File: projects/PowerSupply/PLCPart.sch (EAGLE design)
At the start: 29 parts, among them IC1 L7818CV, IC2 L7918CV, IC3 LM741P, IC4 LM741P, IC5 L7915CV, IC6 L7815CV, X1 MCU-PWR, X2 MCU-IN, X3 MCU-OUT

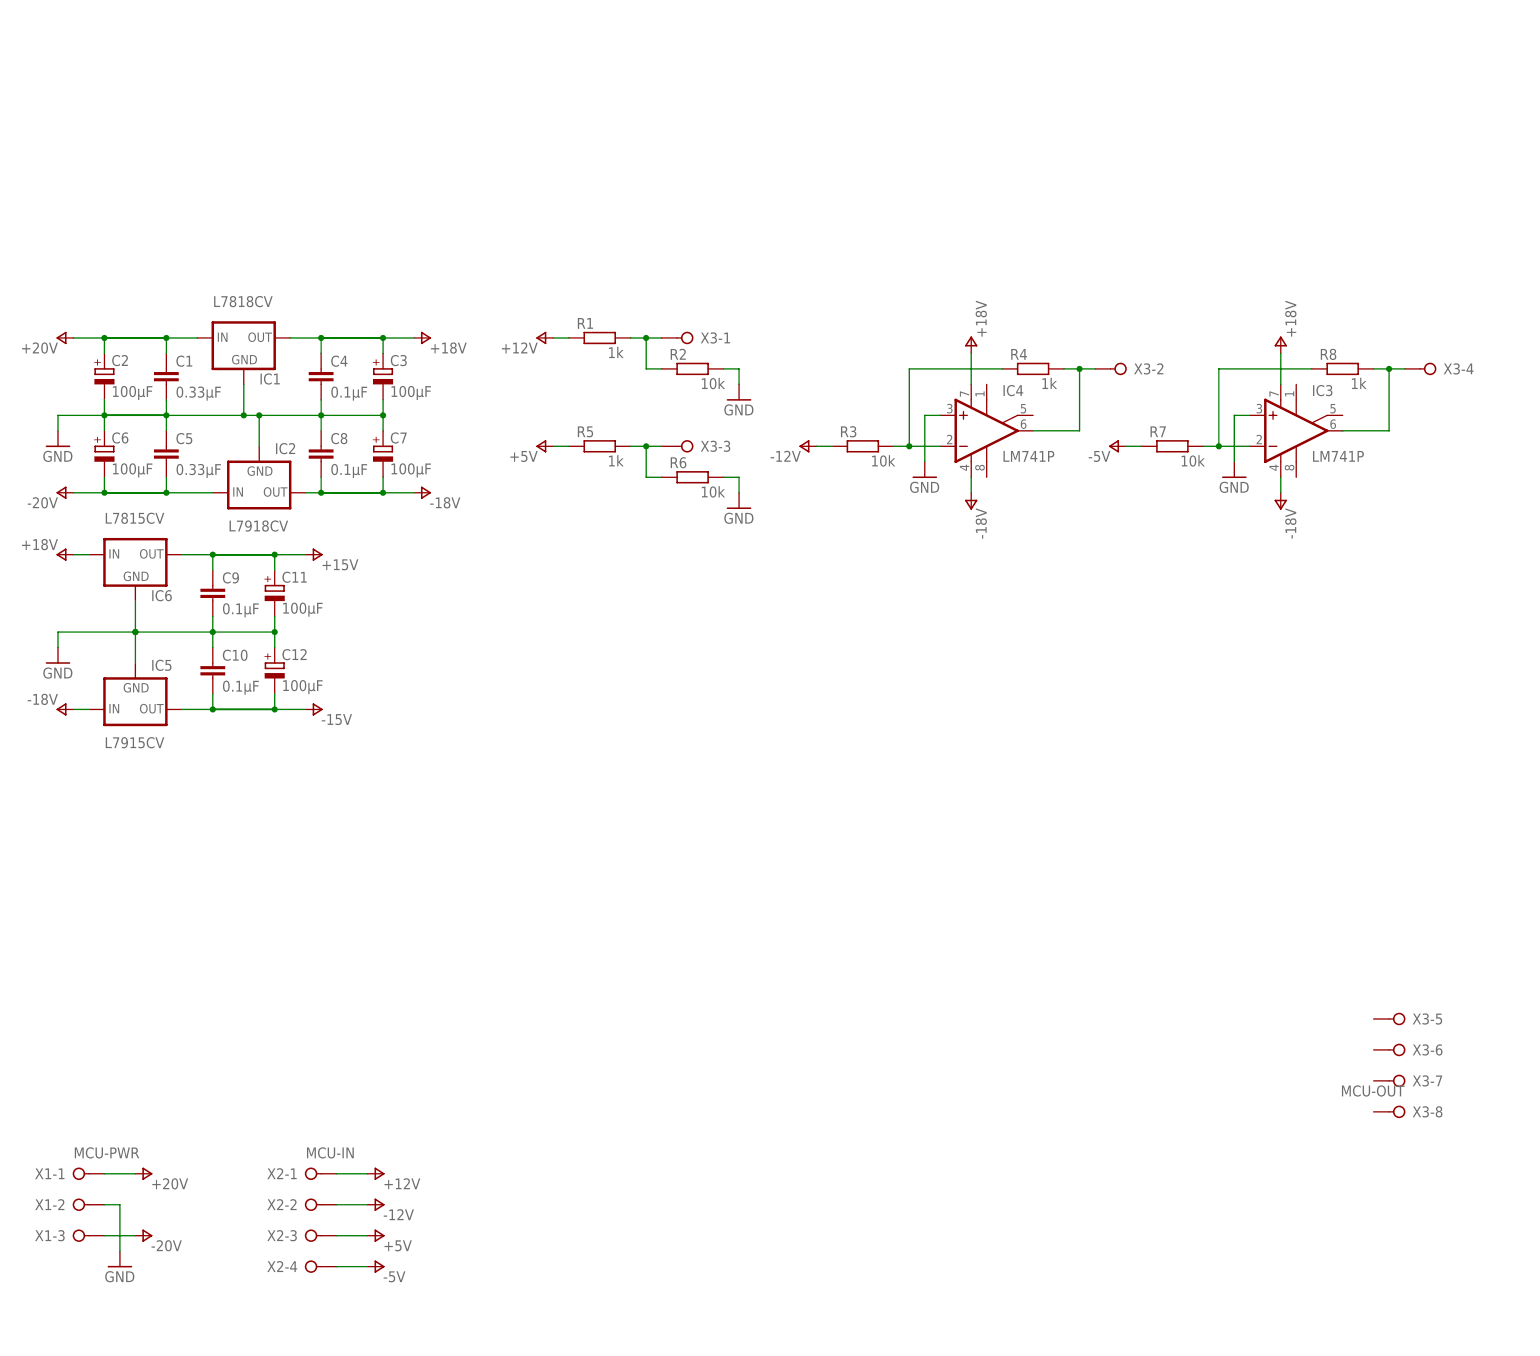
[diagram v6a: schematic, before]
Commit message: feat: plc part op amps (lm358) added
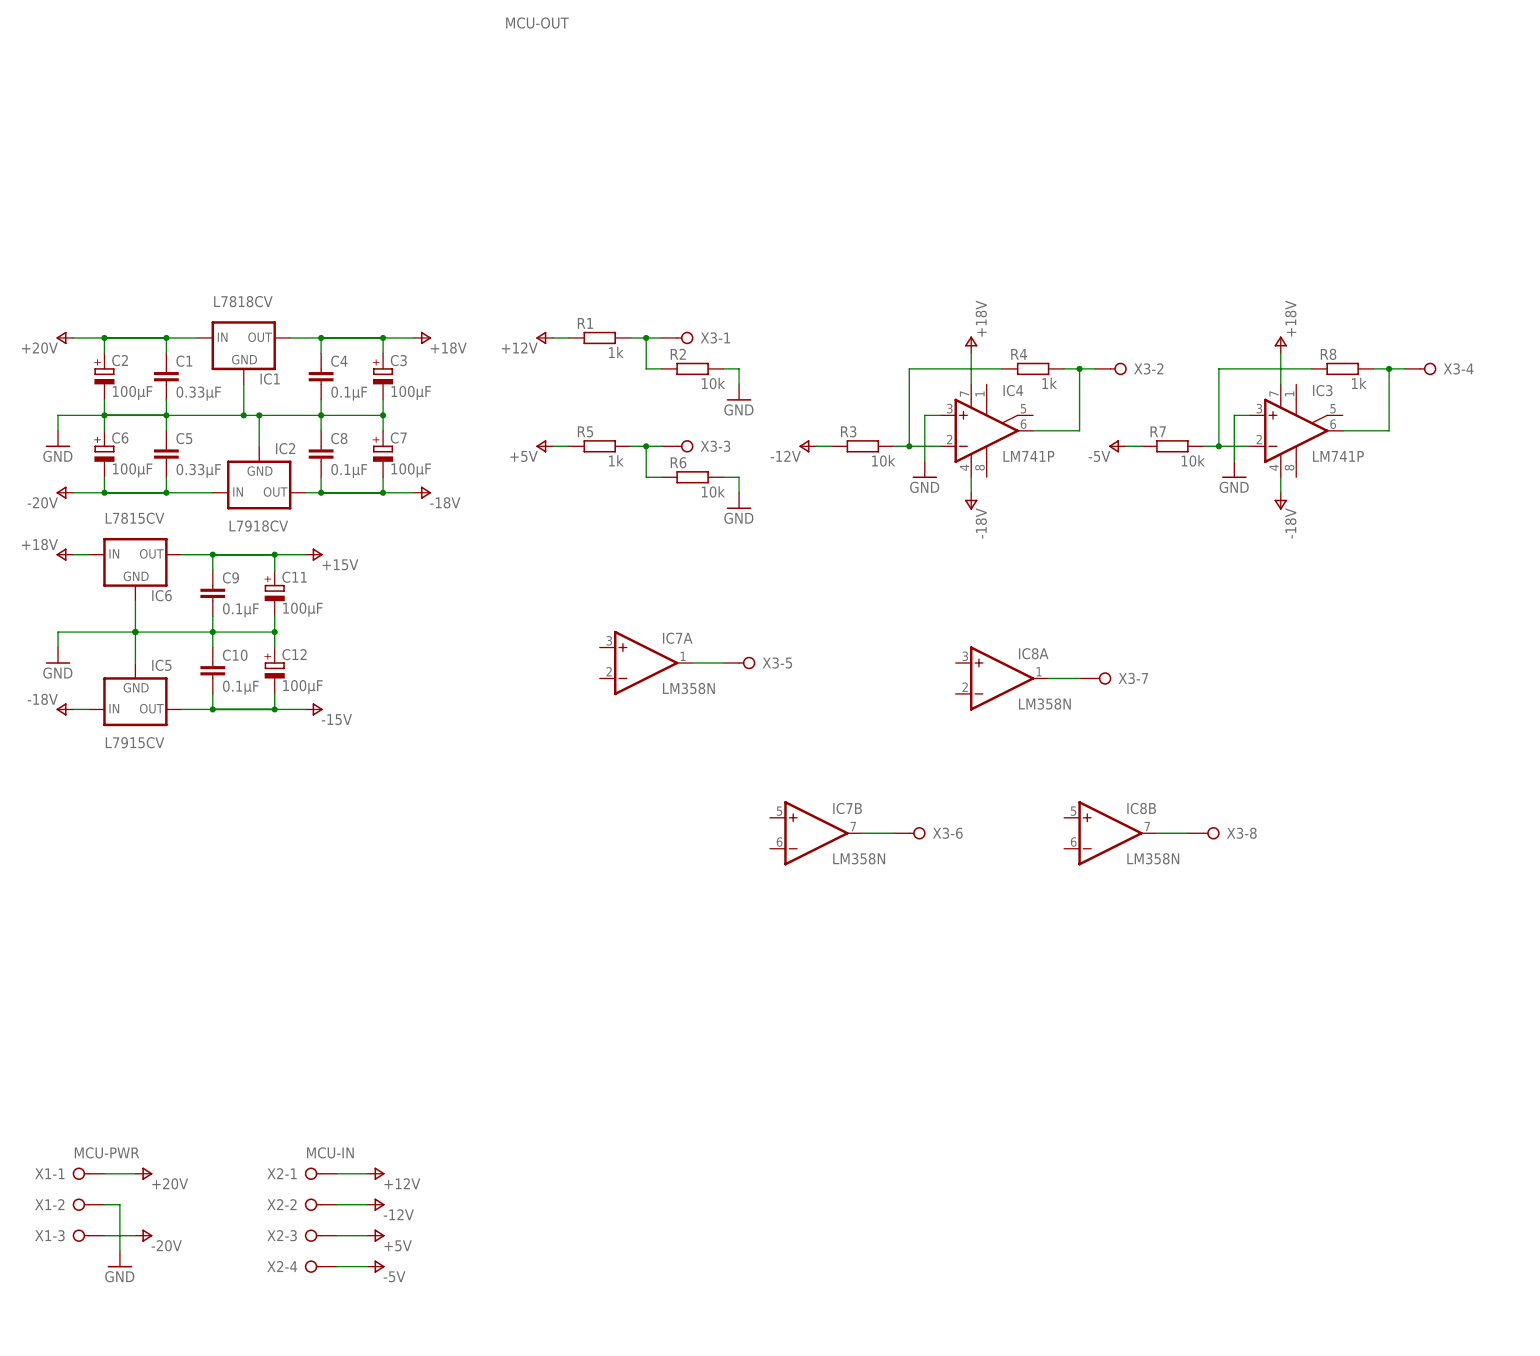
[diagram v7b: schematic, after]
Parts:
- added IC7, IC8: LM358N, linear:LM358N
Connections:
- new net N$10: IC8B.OUT, X3-8.KL
- new net N$7: IC7A.OUT, X3-5.KL
- new net N$8: IC7B.OUT, X3-6.KL
- new net N$9: IC8A.OUT, X3-7.KL
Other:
- moved on the sheet: X3-5, X3-6, X3-7, X3-8
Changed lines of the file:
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@@
 <part name="P+10" library="bb84-supply" deviceset="+15V" device=""/>
 <part name="P-10" library="bb84-supply" deviceset="-15V" device=""/>
+<part name="IC7" library="linear" library_urn="urn:adsk.eagle:library:262" deviceset="LM358" device="N" package3d_urn="urn:adsk.eagle:package:16409/2"/>
+<part name="IC8" library="linear" library_urn="urn:adsk.eagle:library:262" deviceset="LM358" device="N" package3d_urn="urn:adsk.eagle:package:16409/2"/>
 </parts>
 <sheets>
@@
 <attribute name="NAME" x="242.57" y="163.449" size="1.778" layer="95" rot="MR180"/>
 </instance>
-<instance part="X3" gate="-5" x="236.22" y="55.88" smashed="yes" rot="MR0">
-<attribute name="NAME" x="237.49" y="56.769" size="1.778" layer="95" rot="MR180"/>
-</instance>
-<instance part="X3" gate="-6" x="236.22" y="50.8" smashed="yes" rot="MR0">
-<attribute name="NAME" x="237.49" y="51.689" size="1.778" layer="95" rot="MR180"/>
-</instance>
-<instance part="X3" gate="-7" x="236.22" y="45.72" smashed="yes" rot="MR0">
-<attribute name="NAME" x="237.49" y="46.609" size="1.778" layer="95" rot="MR180"/>
-</instance>
-<instance part="X3" gate="-8" x="236.22" y="40.64" smashed="yes" rot="MR0">
-<attribute name="VALUE" x="236.22" y="43.18" size="1.778" layer="96" rot="MR0"/>
-<attribute name="NAME" x="237.49" y="41.529" size="1.778" layer="95" rot="MR180"/>
+<instance part="X3" gate="-5" x="129.54" y="114.3" smashed="yes" rot="MR0">
+<attribute name="NAME" x="130.81" y="115.189" size="1.778" layer="95" rot="MR180"/>
+</instance>
+<instance part="X3" gate="-6" x="157.48" y="86.36" smashed="yes" rot="MR0">
+<attribute name="NAME" x="158.75" y="87.249" size="1.778" layer="95" rot="MR180"/>
+</instance>
+<instance part="X3" gate="-7" x="187.96" y="111.76" smashed="yes" rot="MR0">
+<attribute name="NAME" x="189.23" y="112.649" size="1.778" layer="95" rot="MR180"/>
+</instance>
+<instance part="X3" gate="-8" x="205.74" y="86.36" smashed="yes" rot="MR0">
+<attribute name="VALUE" x="99.06" y="218.44" size="1.778" layer="96" rot="MR0"/>
+<attribute name="NAME" x="207.01" y="87.249" size="1.778" layer="95" rot="MR180"/>
 </instance>
 <instance part="P+8" gate="G$1" x="93.98" y="167.64" smashed="yes" rot="MR270">
@@
 <instance part="P-10" gate="G$1" x="58.42" y="106.68" smashed="yes" rot="R90">
 <attribute name="VALUE" x="58.42" y="104.14" size="1.778" layer="96"/>
+</instance>
+<instance part="IC7" gate="A" x="111.76" y="114.3" smashed="yes">
+<attribute name="NAME" x="114.3" y="117.475" size="1.778" layer="95"/>
+<attribute name="VALUE" x="114.3" y="109.22" size="1.778" layer="96"/>
+</instance>
+<instance part="IC7" gate="B" x="139.7" y="86.36" smashed="yes">
+<attribute name="NAME" x="142.24" y="89.535" size="1.778" layer="95"/>
+<attribute name="VALUE" x="142.24" y="81.28" size="1.778" layer="96"/>
+</instance>
+<instance part="IC8" gate="A" x="170.18" y="111.76" smashed="yes">
+<attribute name="NAME" x="172.72" y="114.935" size="1.778" layer="95"/>
+<attribute name="VALUE" x="172.72" y="106.68" size="1.778" layer="96"/>
+</instance>
+<instance part="IC8" gate="B" x="187.96" y="86.36" smashed="yes">
+<attribute name="NAME" x="190.5" y="89.535" size="1.778" layer="95"/>
+<attribute name="VALUE" x="190.5" y="81.28" size="1.778" layer="96"/>
 </instance>
 </instances>
@@
 </segment>
 </net>
+<net name="N$7" class="0">
+<segment>
+<pinref part="IC7" gate="A" pin="OUT"/>
+<pinref part="X3" gate="-5" pin="KL"/>
+<wire x1="119.38" y1="114.3" x2="124.46" y2="114.3" width="0.1524" layer="91"/>
+</segment>
+</net>
+<net name="N$8" class="0">
+<segment>
+<pinref part="X3" gate="-6" pin="KL"/>
+<pinref part="IC7" gate="B" pin="OUT"/>
+<wire x1="152.4" y1="86.36" x2="147.32" y2="86.36" width="0.1524" layer="91"/>
+</segment>
+</net>
+<net name="N$9" class="0">
+<segment>
+<pinref part="IC8" gate="A" pin="OUT"/>
+<pinref part="X3" gate="-7" pin="KL"/>
+<wire x1="177.8" y1="111.76" x2="182.88" y2="111.76" width="0.1524" layer="91"/>
+</segment>
+</net>
+<net name="N$10" class="0">
+<segment>
+<pinref part="IC8" gate="B" pin="OUT"/>
+<pinref part="X3" gate="-8" pin="KL"/>
+<wire x1="195.58" y1="86.36" x2="200.66" y2="86.36" width="0.1524" layer="91"/>
+</segment>
+</net>
 </nets>
 </sheet>
 </sheets>
+<errors>
+</errors>
 </schematic>
 </drawing>

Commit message: feat: plc part modified
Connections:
- net +15V: now also IC7P.V+, IC8P.V+
- net -15V: now also IC7P.V-, IC8P.V-
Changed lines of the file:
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@@
 <part name="IC7" library="linear" library_urn="urn:adsk.eagle:library:262" deviceset="LM358" device="N" package3d_urn="urn:adsk.eagle:package:16409/2"/>
 <part name="IC8" library="linear" library_urn="urn:adsk.eagle:library:262" deviceset="LM358" device="N" package3d_urn="urn:adsk.eagle:package:16409/2"/>
+<part name="P+12" library="bb84-supply" deviceset="+15V" device=""/>
+<part name="P-12" library="bb84-supply" deviceset="-15V" device=""/>
+<part name="P+13" library="bb84-supply" deviceset="+15V" device=""/>
+<part name="P-13" library="bb84-supply" deviceset="-15V" device=""/>
 </parts>
 <sheets>
@@
 </instance>
 <instance part="X3" gate="-8" x="205.74" y="86.36" smashed="yes" rot="MR0">
-<attribute name="VALUE" x="99.06" y="218.44" size="1.778" layer="96" rot="MR0"/>
+<attribute name="VALUE" x="129.54" y="172.72" size="1.778" layer="96" rot="MR0"/>
 <attribute name="NAME" x="207.01" y="87.249" size="1.778" layer="95" rot="MR180"/>
 </instance>
@@
 <attribute name="NAME" x="190.5" y="89.535" size="1.778" layer="95"/>
 <attribute name="VALUE" x="190.5" y="81.28" size="1.778" layer="96"/>
+</instance>
+<instance part="IC7" gate="P" x="134.62" y="22.86" smashed="yes"/>
+<instance part="P+12" gate="G$1" x="134.62" y="35.56" smashed="yes">
+<attribute name="VALUE" x="137.16" y="35.56" size="1.778" layer="96" rot="R90"/>
+</instance>
+<instance part="P-12" gate="G$1" x="134.62" y="10.16" smashed="yes" rot="MR0">
+<attribute name="VALUE" x="137.16" y="10.16" size="1.778" layer="96" rot="MR270"/>
+</instance>
+<instance part="IC8" gate="P" x="139.7" y="22.86" smashed="yes"/>
+<instance part="P+13" gate="G$1" x="139.7" y="35.56" smashed="yes">
+<attribute name="VALUE" x="142.24" y="35.56" size="1.778" layer="96" rot="R90"/>
+</instance>
+<instance part="P-13" gate="G$1" x="139.7" y="10.16" smashed="yes" rot="MR0">
+<attribute name="VALUE" x="142.24" y="10.16" size="1.778" layer="96" rot="MR270"/>
 </instance>
 </instances>
@@
 <pinref part="P+10" gate="G$1" pin="+15V"/>
 </segment>
+<segment>
+<pinref part="P+12" gate="G$1" pin="+15V"/>
+<pinref part="IC7" gate="P" pin="V+"/>
+<wire x1="134.62" y1="33.02" x2="134.62" y2="30.48" width="0.1524" layer="91"/>
+</segment>
+<segment>
+<pinref part="IC8" gate="P" pin="V+"/>
+<pinref part="P+13" gate="G$1" pin="+15V"/>
+<wire x1="139.7" y1="30.48" x2="139.7" y2="33.02" width="0.1524" layer="91"/>
+</segment>
 </net>
 <net name="-15V" class="0">
@@
 <pinref part="P-10" gate="G$1" pin="-15V"/>
 </segment>
-</net>
+<segment>
+<pinref part="IC7" gate="P" pin="V-"/>
+<pinref part="P-12" gate="G$1" pin="-15V"/>
+<wire x1="134.62" y1="15.24" x2="134.62" y2="12.7" width="0.1524" layer="91"/>
+</segment>
+<segment>
+<pinref part="P-13" gate="G$1" pin="-15V"/>
+<pinref part="IC8" gate="P" pin="V-"/>
+<wire x1="139.7" y1="12.7" x2="139.7" y2="15.24" width="0.1524" layer="91"/>
+</segment>
+</net>
